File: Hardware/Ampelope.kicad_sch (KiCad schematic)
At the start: 35 parts, among them J1 IN_A, J2 IN_B, J3 RM_OUT, J4 Eurorack_10_pin_power, U1 MC1496, U2 TL072

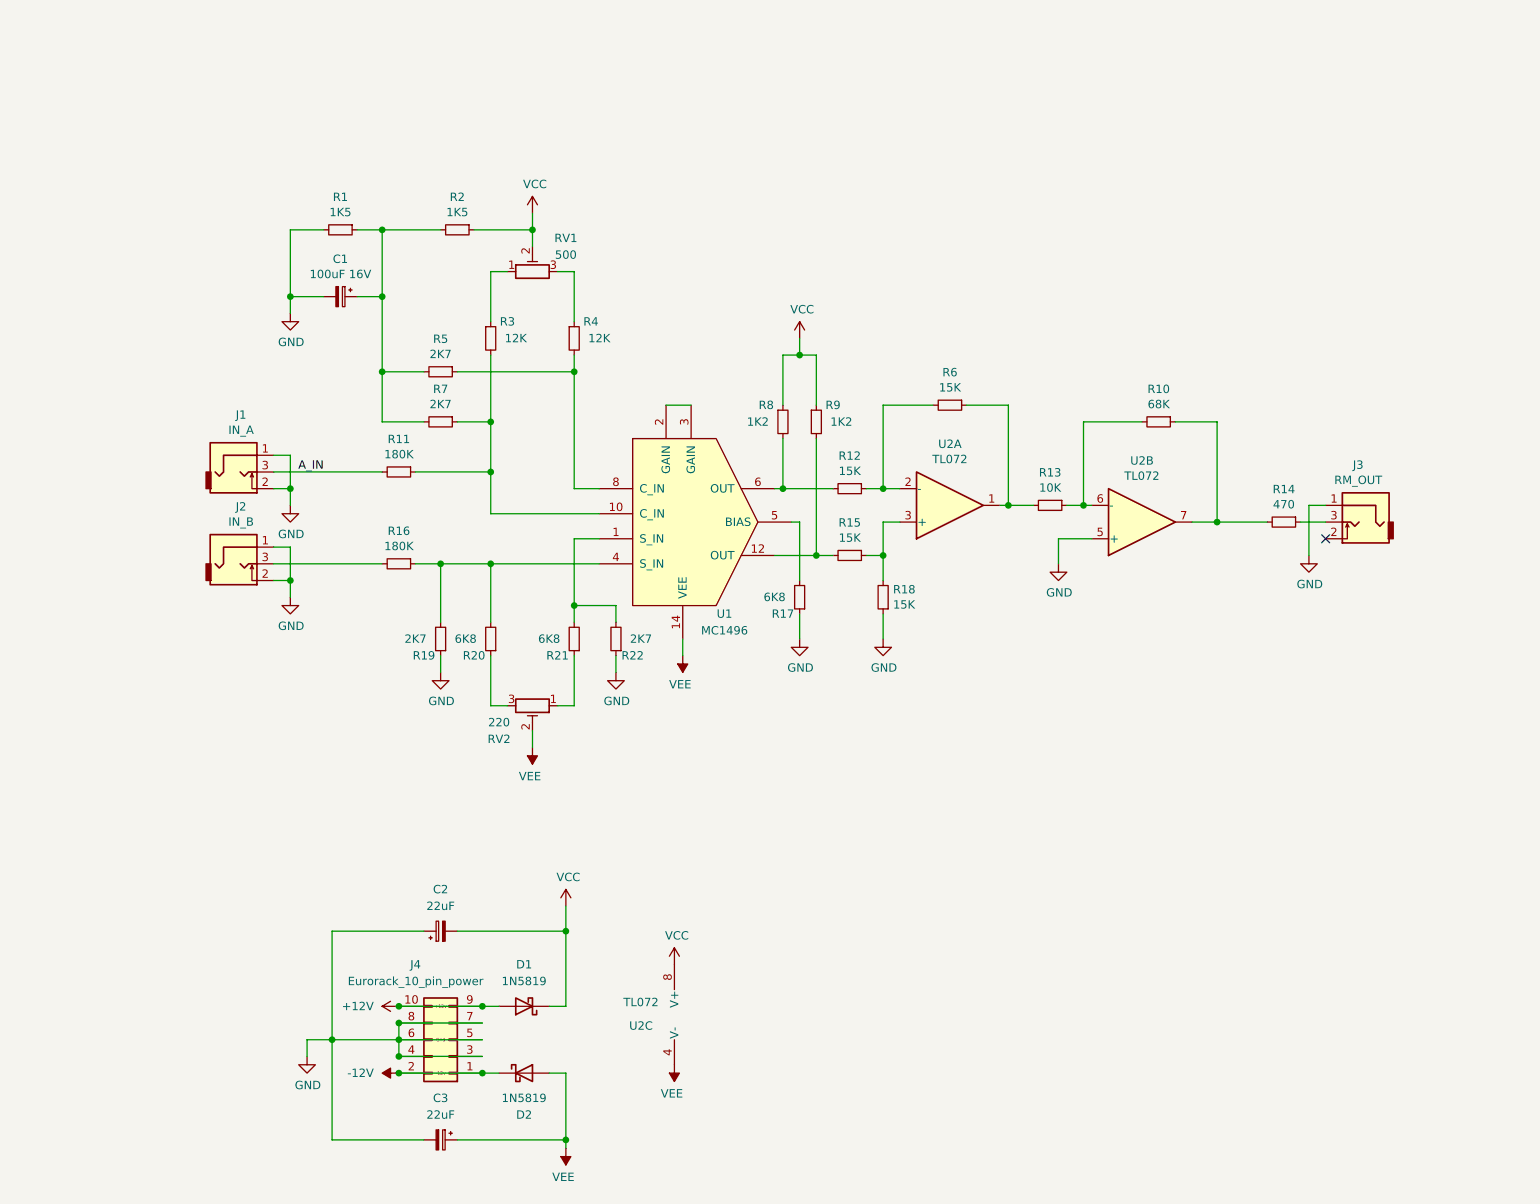
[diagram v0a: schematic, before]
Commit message: Added STM32G431 project; clock configuration complete
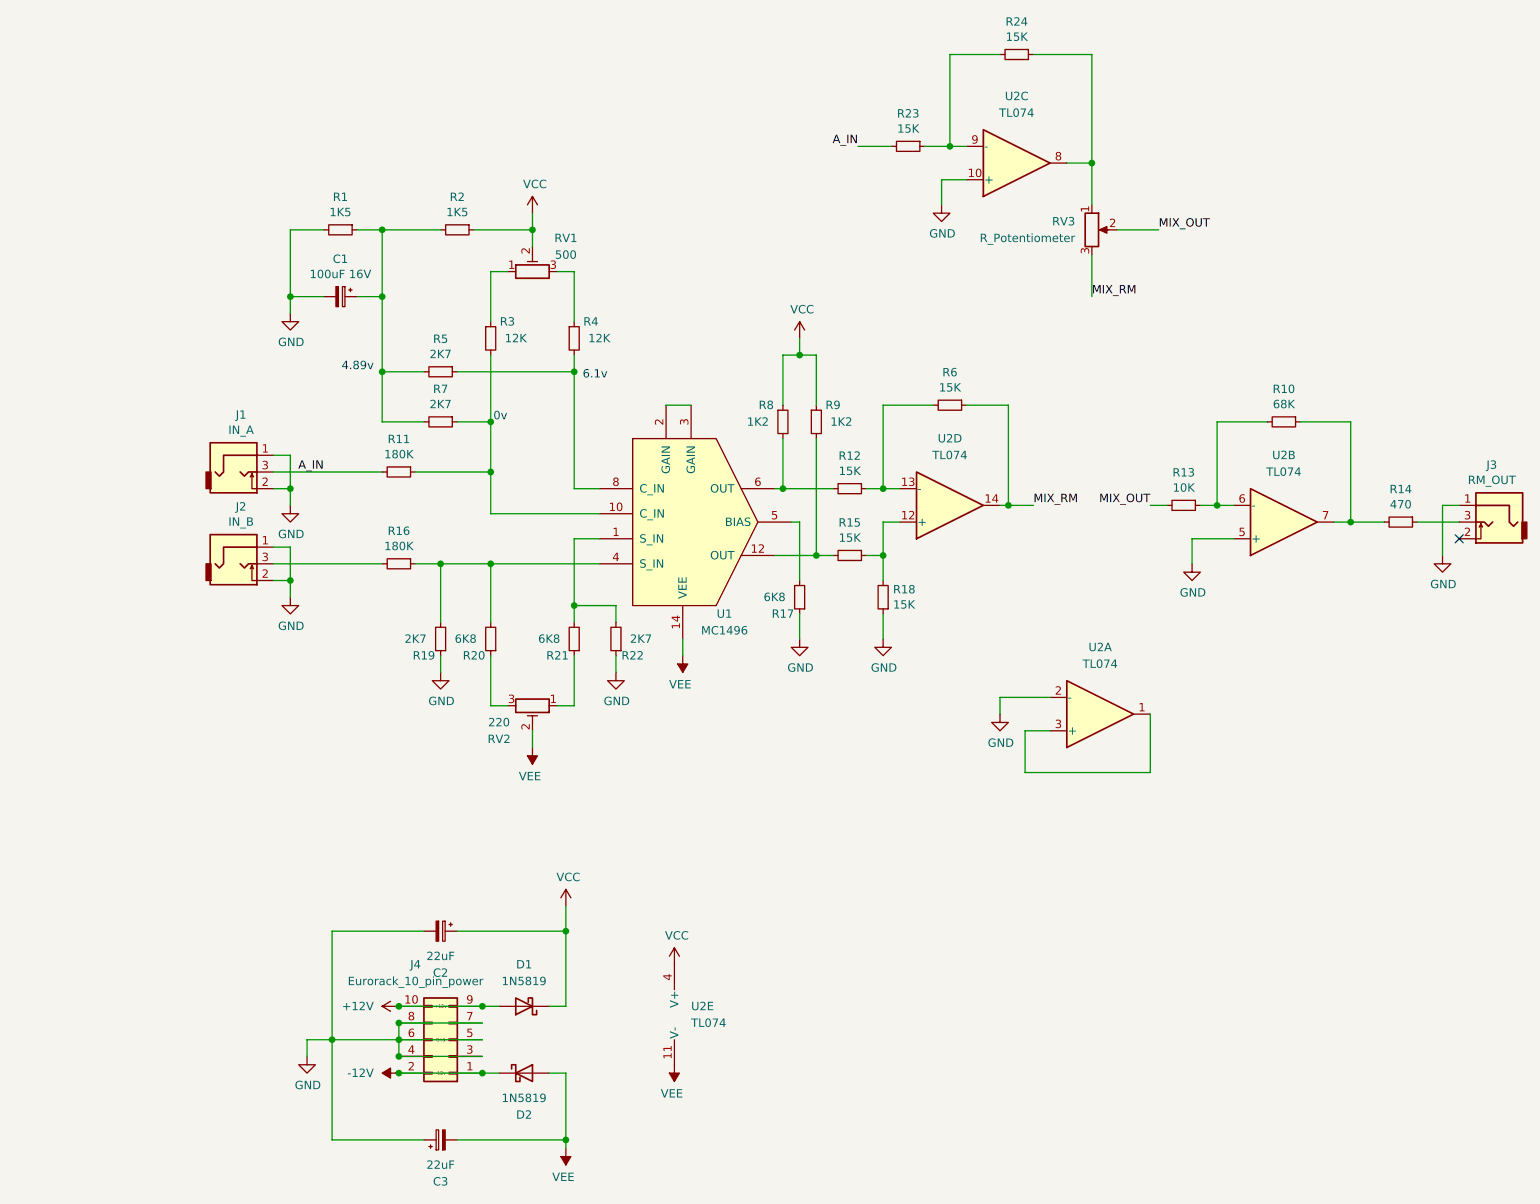
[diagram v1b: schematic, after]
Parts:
- removed U2: TL072, Package_SO:SOIC-8_3.9x4.9mm_P1.27mm, symbol Amplifier_Operational:TL072
- added R23, R24: 15K, Resistor_SMD:R_0603_1608Metric_Pad0.98x0.95mm_HandSolder, symbol Device:R_Small
- added RV3: R_Potentiometer, Custom_Footprints:Alpha_9mm_Potentiometer_Aligned, symbol Device:R_Potentiometer
- added U2: TL074, Package_SO:SOIC-14_3.9x8.7mm_P1.27mm, symbol Amplifier_Operational:TL074
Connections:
- net A_IN: now also R23.2
- net GND: now also C2.2, C3.1, U2.10 (+), U2.2 (-), U2.5 (+); no longer C2.1, C3.2
- net VCC: now also C2.1, U2.4 (V+); no longer C2.2
- net VEE: now also C3.2, U2.11 (V-); no longer C3.1
- net MIX_OUT: now reaches R13.2
- net MIX_OUT: now also RV3.2; no longer R6.1
- net at R12.1, R6.2: now also U2.13 (-)
- net at R15.1, R18.2: now also U2.12 (+)
- net at R10.2, R13.1: now also U2.6 (-)
- net at R10.1, R14.2: now also U2.7
- new net: R24.1, RV3.1, U2.8
- new net: R23.1, R24.2, U2.9 (-)
- new net: U2.1, U2.3 (+)
- new net MIX_RM: R6.1, RV3.3, U2.14
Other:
- note added: "0v"
- note added: "4.89v"
- note added: "6.1v"
- moved on the sheet: C2, C3, J3, R10, R13, R14

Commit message: Started implementing ADSR Code
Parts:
- removed C1: 100uF 16V, Capacitor_SMD:CP_Elec_5x5.7, symbol Device:CP_Small
- removed R16: 180K, Resistor_SMD:R_0603_1608Metric_Pad0.98x0.95mm_HandSolder, symbol Device:R_Small
- removed R19, R22: 2K7, Resistor_SMD:R_0603_1608Metric_Pad0.98x0.95mm_HandSolder, symbol Device:R_Small
- removed R20, R21: 6K8, Resistor_SMD:R_0603_1608Metric_Pad0.98x0.95mm_HandSolder, symbol Device:R_Small
- removed R23, R24: 15K, Resistor_SMD:R_0603_1608Metric_Pad0.98x0.95mm_HandSolder, symbol Device:R_Small
- removed RV1: 500, Potentiometer_THT:Potentiometer_Runtron_RM-065_Vertical, symbol Device:R_POT_TRIM
- removed RV2: 220, Potentiometer_THT:Potentiometer_Runtron_RM-065_Vertical, symbol Device:R_POT_TRIM
- removed RV3: R_Potentiometer, Custom_Footprints:Alpha_9mm_Potentiometer_Aligned, symbol Device:R_Potentiometer
- removed unit 3 of U2
- removed unit 4 of U2
- added C1, C4: 1uF, symbol Device:C_Small
- added P1, P2: 100k, symbol Device:R_Potentiometer_Trim
- added Q?: BC547, Package_TO_SOT_THT:TO-92_Inline, symbol Transistor_BJT:BC547
- added R10, R6, R?: 100k, symbol Device:R_Small
- added R8, R9: 1k, symbol Device:R_Small
- added R?: 10k, symbol Device:R_Small
- added unit 4 of U1
- added unit 3 of U1
- J1: value IN_A -> B_In; footprint Custom_Footprints:THONKICONN_hole -> (none)
- J2: value IN_B -> A_In; footprint Custom_Footprints:THONKICONN_hole -> (none)
- R1: value 1K5 -> 47k; footprint Resistor_SMD:R_0603_1608Metric_Pad0.98x0.95mm_HandSolder -> (none)
- R11: value 180K -> 4k7
- R13: renamed from R17; value 6K8 -> 4k7
- R2: value 1K5 -> 1k; footprint Resistor_SMD:R_0603_1608Metric_Pad0.98x0.95mm_HandSolder -> (none)
- R3: value 12K -> 1k; footprint Resistor_SMD:R_0603_1608Metric_Pad0.98x0.95mm_HandSolder -> (none)
- R4: value 12K -> 120k; footprint Resistor_SMD:R_0603_1608Metric_Pad0.98x0.95mm_HandSolder -> (none)
- R5: value 2K7 -> 120k; footprint Resistor_SMD:R_0603_1608Metric_Pad0.98x0.95mm_HandSolder -> (none)
- R7: value 2K7 -> 1k; footprint Resistor_SMD:R_0603_1608Metric_Pad0.98x0.95mm_HandSolder -> (none)
- renumbered J4 to J3, J3 to J4, R8 to R12, R9 to R14, R12 to R15, R15 to R16, R18 to R17, R6 to R18, R13 to R19, R10 to R20, R14 to R21, U2 to U1, U1 to U2
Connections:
- net MIX_OUT is gone; now on an unnamed net: R19.2
- net MIX_RM is gone; now on an unnamed net: R18.1
- net +12V: now also R2.2, R4.2, R7.2, P1.1
- net -12V: now also R5.2, P1.3
- net GND: now also R3.2, R10.1, R8.1, R?.1, U1.12 (+); no longer J1.2, J2.2, R1.2, U1.2 (-)
- net VCC: now also Q?.1 (C); no longer R2.1
- net VEE: now also R?.1
- net at J2.3: now also C1.2
- net B_Bias: now reaches U2.1 (S_IN)
- net B_Bias: now also P2.2
- net at U2.2 (GAIN): now also R11.2; no longer U2.3 (GAIN)
- net at U2.4 (S_IN): now also R10.2, R9.2
- net A_Bias: now reaches R3.1
- net A_Bias: now also R1.2, R2.1, U2.10 (C_IN)
- net at R4.1: now also P2.1
- net at R15.1: now also R17.2, U1.3 (+); no longer R18.2
- net at R16.1: now also R18.2, U1.2 (-); no longer R17.2
- net at U1.1: no longer U1.3 (+)
- net A_IN renamed B_Input
- net B_Input: now also Q?.2 (B), R?.2, U1.10 (+); no longer R11.2
- new net: R11.1, U2.3 (GAIN)
- new net: R6.2, R7.1, R8.2, U2.8 (C_IN)
- new net: C4.1, R9.1
- new net: P1.2, R1.1
- new net: C1.1, R6.1
- new net: U1.13 (-), U1.14
- new net: P2.3, R5.1
- new net Either_Buffer: C4.2
- new net OpAmp_Buffer: U1.8, U1.9 (-)
- new net Transistor_Buffer: Q?.3 (E), R?.2
- no-connect marks 1 -> 3
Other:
- note removed: "0v"
- note removed: "4.89v"
- note removed: "6.1v"
- moved on the sheet: J4, R18, R19, R20, R21, U1A, U1B

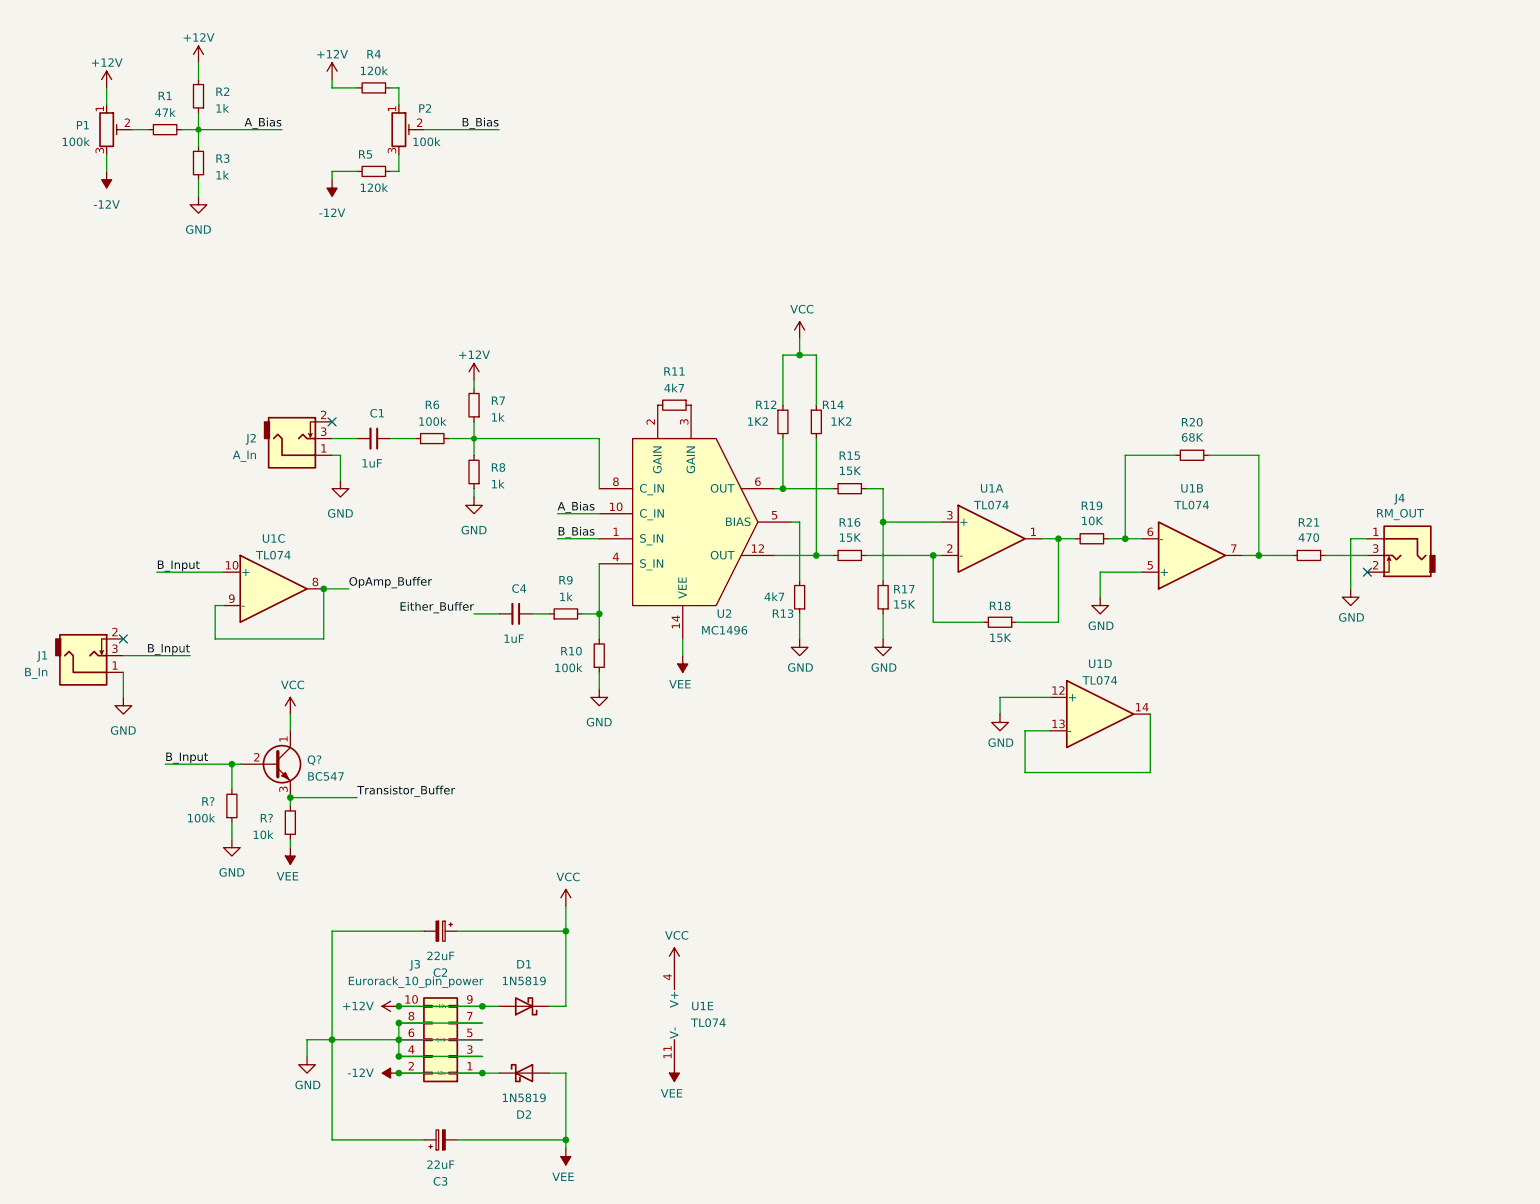
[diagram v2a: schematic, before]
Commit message: Started schematic; basic envelope working on timer
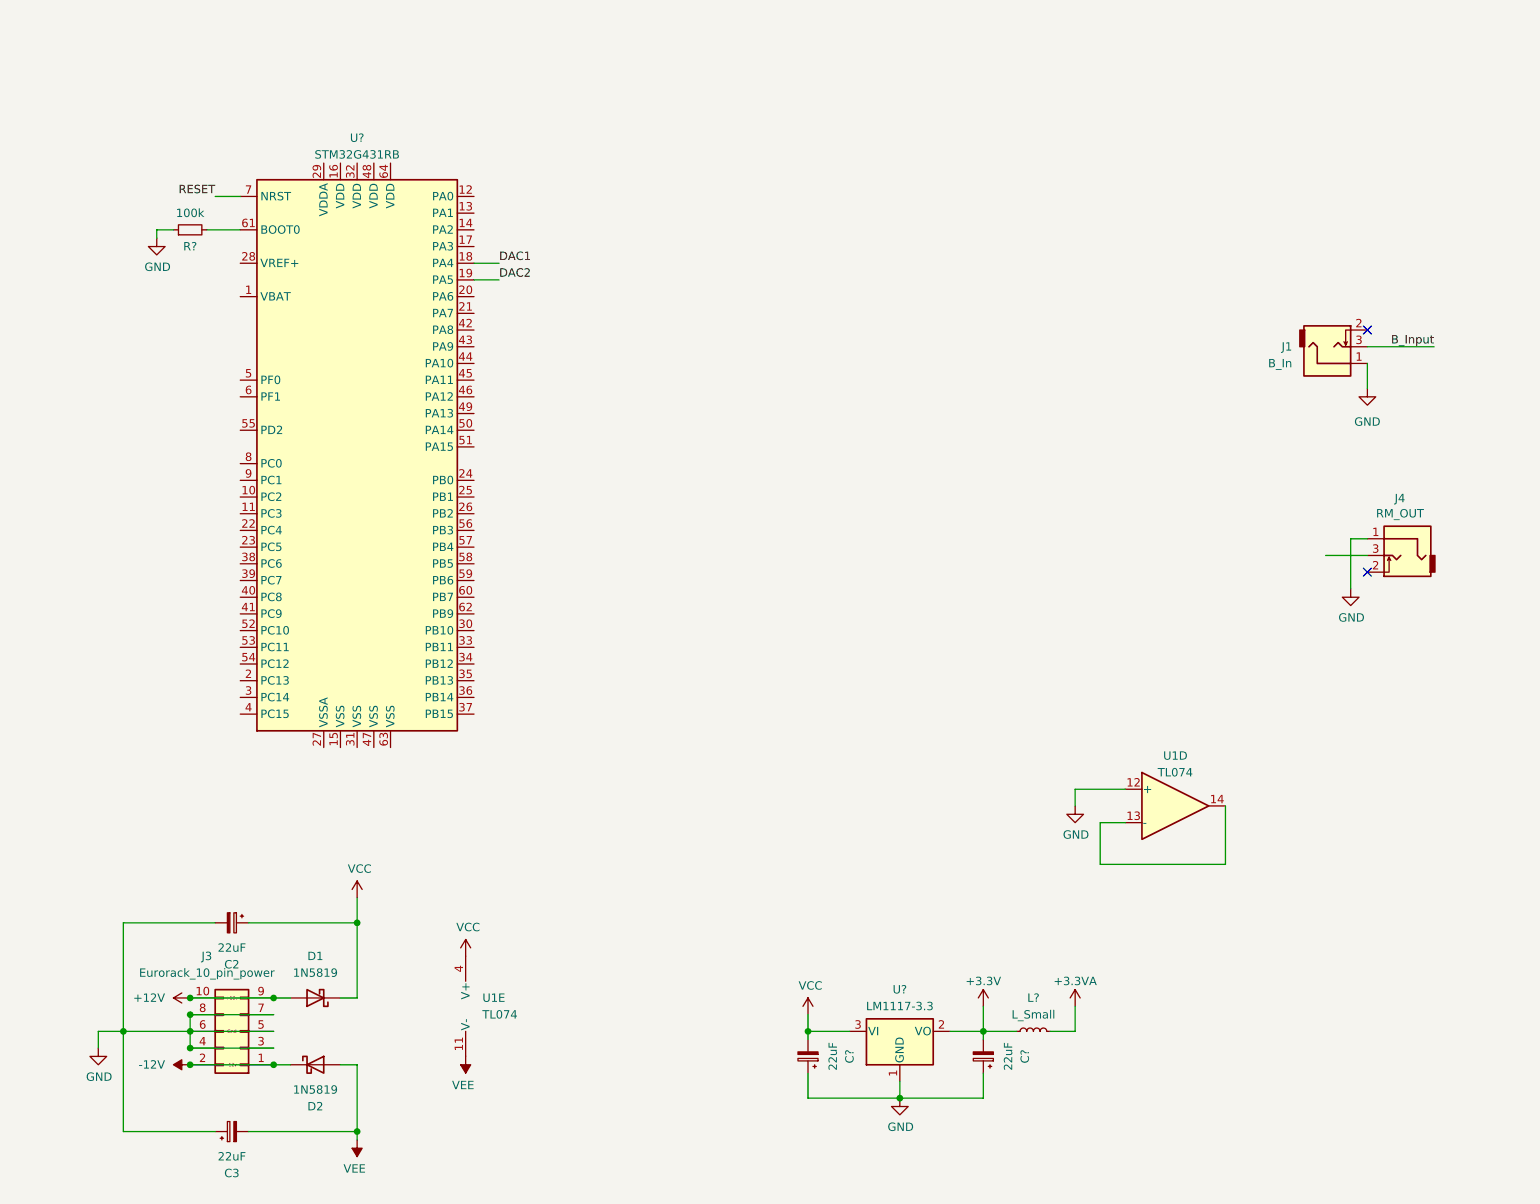
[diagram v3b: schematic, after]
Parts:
- removed C1, C4: 1uF, symbol Device:C_Small
- removed J2: A_In, symbol thonkiconn:AudioJack2_Ground_Switch
- removed P1, P2: 100k, symbol Device:R_Potentiometer_Trim
- removed Q?: BC547, Package_TO_SOT_THT:TO-92_Inline, symbol Transistor_BJT:BC547
- removed R1: 47k, symbol Device:R_Small
- removed R10, R6, R?: 100k, symbol Device:R_Small
- removed R11, R13: 4k7, Resistor_SMD:R_0603_1608Metric_Pad0.98x0.95mm_HandSolder, symbol Device:R_Small
- removed R12, R14: 1K2, Resistor_SMD:R_0603_1608Metric_Pad0.98x0.95mm_HandSolder, symbol Device:R_Small
- removed R15, R16, R17, R18: 15K, Resistor_SMD:R_0603_1608Metric_Pad0.98x0.95mm_HandSolder, symbol Device:R_Small
- removed R19: 10K, Resistor_SMD:R_0603_1608Metric_Pad0.98x0.95mm_HandSolder, symbol Device:R_Small
- removed R2, R3, R7, R8, R9: 1k, symbol Device:R_Small
- removed R20: 68K, Resistor_SMD:R_0603_1608Metric_Pad0.98x0.95mm_HandSolder, symbol Device:R_Small
- removed R21: 470, Resistor_SMD:R_0603_1608Metric_Pad0.98x0.95mm_HandSolder, symbol Device:R_Small
- removed R4, R5: 120k, symbol Device:R_Small
- removed R?: 10k, symbol Device:R_Small
- removed unit 2 of U1
- removed unit 1 of U1
- removed unit 3 of U1
- removed U2: MC1496, Package_SO:SOIC-14_3.9x8.7mm_P1.27mm, symbol MC1496:MC1496
- added C? (x2): 22uF, Capacitor_SMD:CP_Elec_4x5.8, symbol Encoder:CP_Small
- added L?: L_Small, symbol Device:L_Small
- added R?: 100k, symbol Device:R_Small
- added U?: LM1117-3.3, symbol Regulator_Linear:LM1117-3.3
- added U?: STM32G431RB, Package_QFP:LQFP-64_10x10mm_P0.5mm, symbol STM32G431RB:STM32G431RB
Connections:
- net GND: now also C?.1, C?.1, R?.1, U?.1 (GND)
- net VCC: now also C?.2, U?.3 (VI)
- new net: R?.2, U?.61 (BOOT0)
- new net +3.3VA: L?.2
- new net +3V3: C?.2, L?.1, U?.2 (VO)
- new net DAC1: U?.18 (PA4)
- new net DAC2: U?.19 (PA5)
- new net RESET: U?.7 (NRST)
- no-connect marks 3 -> 2
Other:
- moved on the sheet: C2, C3, D1, D2, J1, J3, U1D, U1E
